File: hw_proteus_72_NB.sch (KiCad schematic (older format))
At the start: 128 parts, among them P1 1123038-2

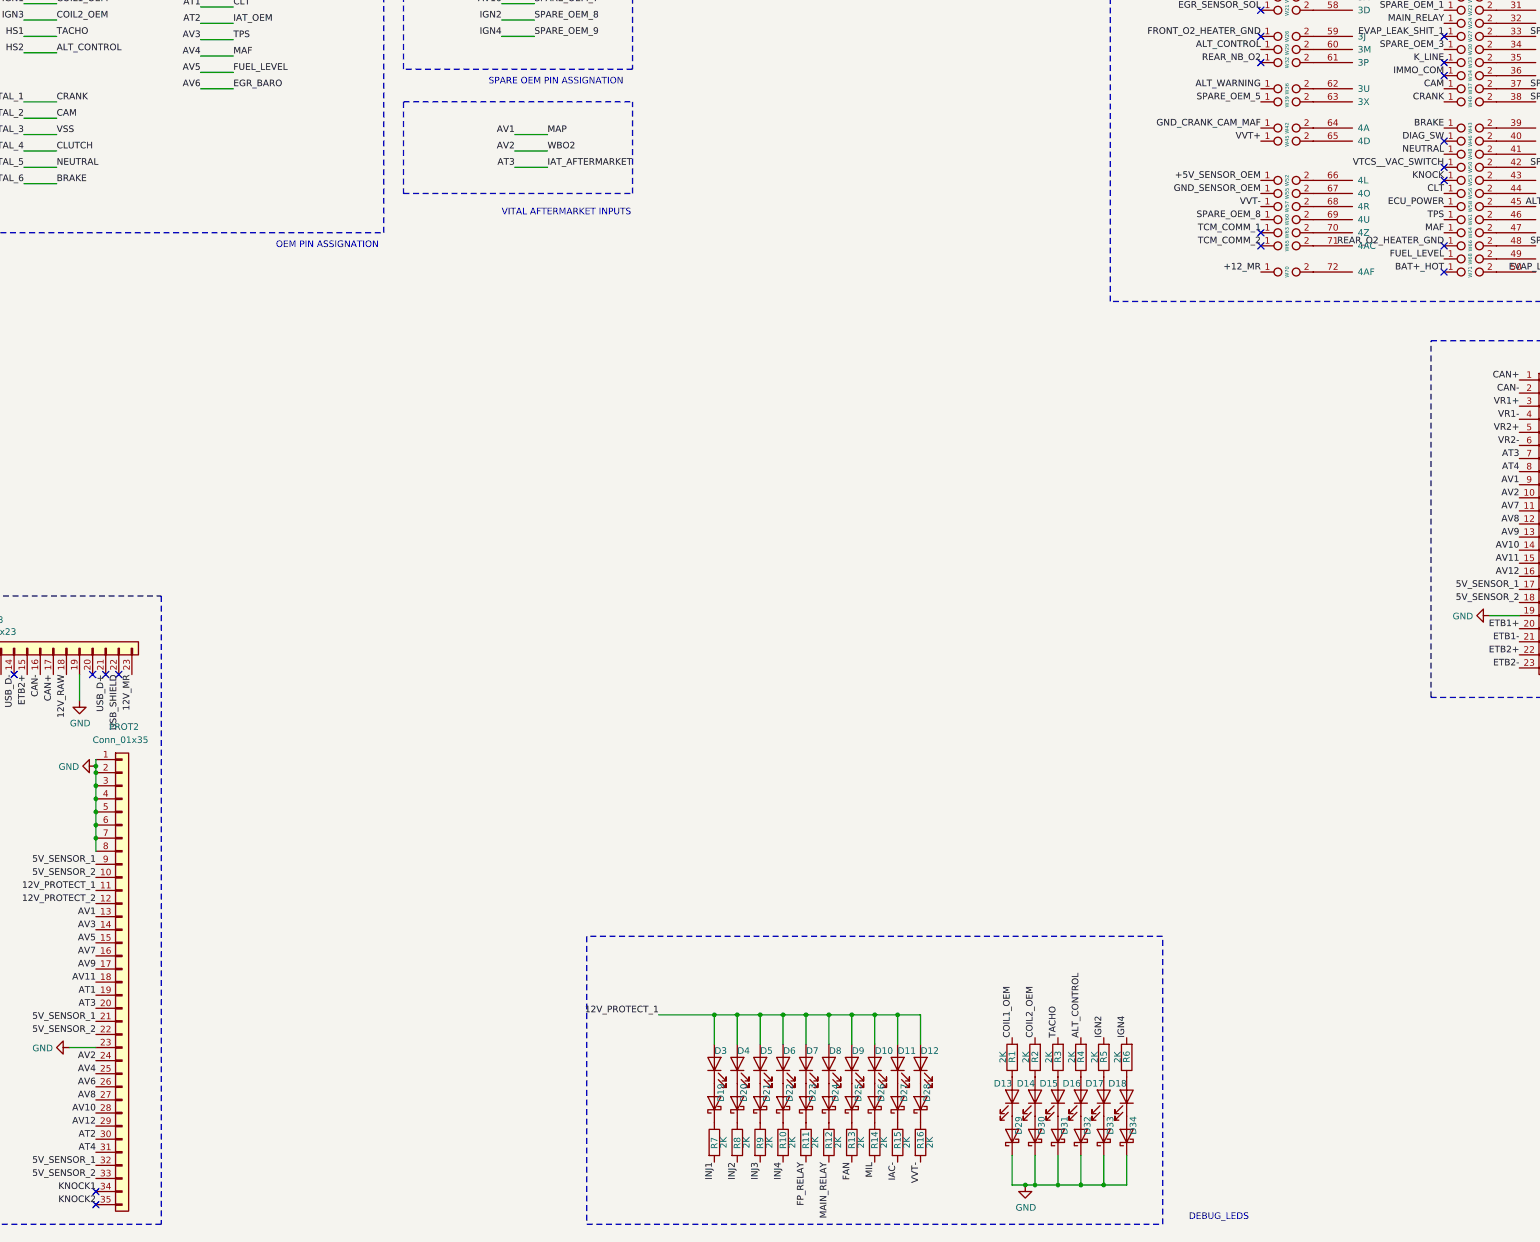
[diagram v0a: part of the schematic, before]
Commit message: Added knock sensing connection
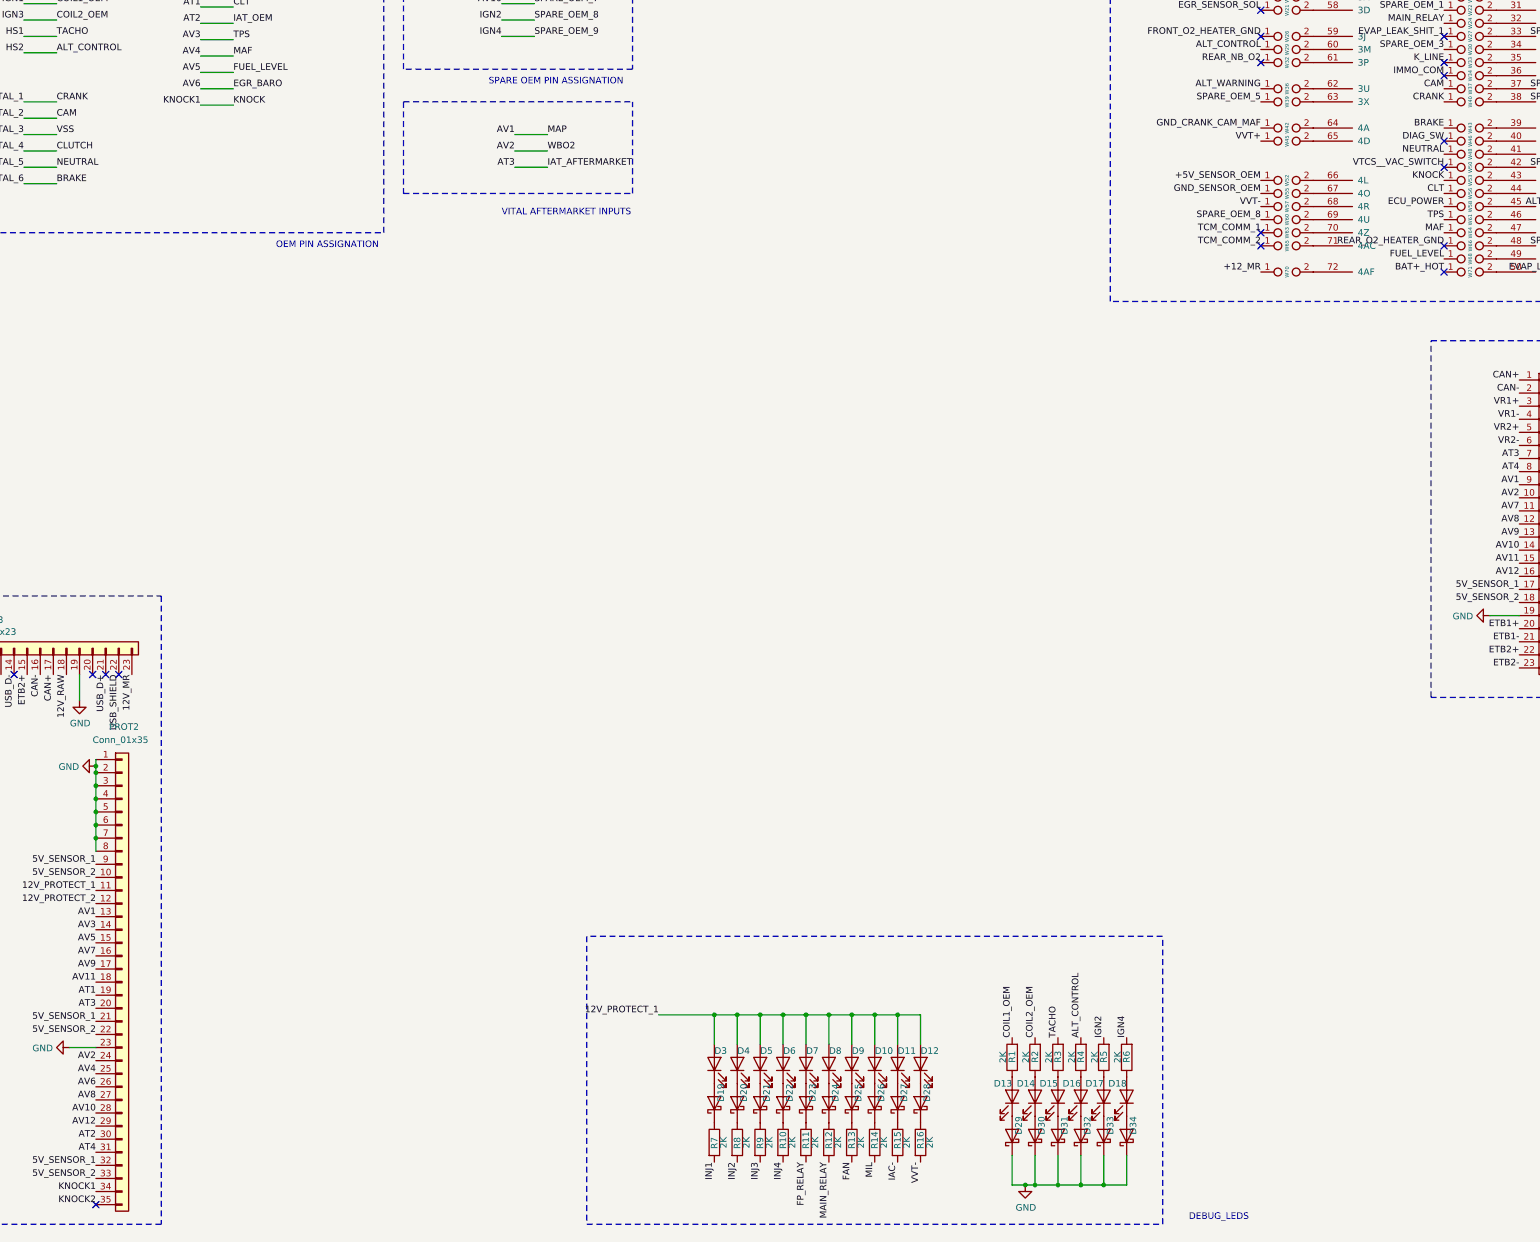
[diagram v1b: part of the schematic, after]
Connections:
- net KNOCK1 is gone; now on net KNOCK: PROT2.34 (Pin_34)
- no-connect marks 33 -> 31
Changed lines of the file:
@@
 NoConn ~ 13100 3800
 NoConn ~ 13100 3600
-NoConn ~ 13100 3100
 NoConn ~ 13100 3000
 NoConn ~ 13100 2800
@@
 NoConn ~ 2175 6875
 NoConn ~ 14250 1000
-NoConn ~ 2800 10825
 NoConn ~ 2800 10925
 $Comp
@@
 Wire Wire Line
 	2250 1000 2500 1000
+Text Label 3600 2525 2    50   ~ 0
+KNOCK1
+Text Label 3850 2525 0    50   ~ 0
+KNOCK
+Wire Wire Line
+	3600 2525 3850 2525
 $EndSCHEMATC

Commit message: switched LS and HS outputs to match hardware timers distribution. Added a 2k pulldown for the tach output"
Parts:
- added R17: 1K, Resistor_SMD:R_0201_0603Metric, symbol Device:R
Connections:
- net ALT_CONTROL: now also PROT1.13 (Pin_13); no longer PROT1.1 (Pin_1)
- net GND: now also R17.1
- net HS1: now also R17.2
- net IAC-: now also PROT1.20 (Pin_20); no longer PROT1.7 (Pin_7)
- net HS3 renamed HS2
- net HS2: now also PROT1.1 (Pin_1); no longer PROT1.13 (Pin_13)
- net LS10 renamed LS7
- net LS7: now also PROT1.7 (Pin_7); no longer PROT1.20 (Pin_20)
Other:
- note added: "PULL-UP/DOWN\n"
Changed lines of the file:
@@
 Wire Notes Line
 	15050 9625 15050 7500
-Text Notes 15225 9725 0    50   ~ 0
-FLYBACK DIODES\n
 $Comp
 L Device:D_Schottky D22
@@
 FP_RELAY
 Text Label 1250 2500 0    50   ~ 0
-IAC-
+MIL
 Text Label 1250 2625 0    50   ~ 0
 ALT_WARNING
@@
 VVT-
 Text Label 1250 2875 0    50   ~ 0
-MIL
+IAC-
 Text Label 1250 3000 0    50   ~ 0
 FAN
@@
 IGN12
 Text Label 15300 6525 2    50   ~ 0
-HS3
+HS2
 Text Label 15300 6625 2    50   ~ 0
 HS4
@@
 HS1
 Text Label 2250 2125 2    50   ~ 0
-HS2
+HS3
 Text Label 2500 1750 0    50   ~ 0
 COIL1_OEM
@@
 Wire Wire Line
 	3600 2525 3850 2525
+Wire Notes Line
+	14650 7475 14650 9475
+Wire Notes Line
+	14650 9475 11475 9475
+Wire Notes Line
+	11475 9475 11475 7475
+Wire Notes Line
+	11475 7475 14650 7475
+Text Notes 15225 9725 0    50   ~ 0
+FLYBACK DIODES\n
+Text Notes 14000 9600 0    50   ~ 0
+PULL-UP/DOWN\n
+Text Label 12500 7750 2    50   ~ 0
+TACHO
+$Comp
+L power:GND #PWR0112
+U 1 1 5E9CA471
+P 13000 7750
+F 0 "#PWR0112" H 13000 7500 50  0001 C CNN
+F 1 "GND" V 13005 7622 50  0000 R CNN
+F 2 "" H 13000 7750 50  0001 C CNN
+F 3 "" H 13000 7750 50  0001 C CNN
+	1    13000 7750
+	0    -1   -1   0
+$EndComp
+$Comp
+L Device:R R17
+U 1 1 5E9CB898
+P 12750 7750
+F 0 "R17" V 12543 7750 50  0000 C CNN
+F 1 "1K" V 12634 7750 50  0000 C CNN
+F 2 "Resistor_SMD:R_0201_0603Metric" V 12680 7750 50  0001 C CNN
+F 3 "~" H 12750 7750 50  0001 C CNN
+	1    12750 7750
+	0    1    1    0
+$EndComp
+Wire Wire Line
+	13000 7750 12900 7750
+Wire Wire Line
+	12600 7750 12500 7750
 $EndSCHEMATC
